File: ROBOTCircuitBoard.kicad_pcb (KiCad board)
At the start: 2 copper layers, 60.5 x 76.5 mm, 18 parts, among them J1 DB15_HighDensity_MountingHoles, J2 DB15_HighDensity_MountingHoles, P1 CONN_01X03, P13 CONN_01X04, P15 CONN_01X04, P2 CONN_01X04, P24 CONN_01X04, P3 CONN_01X04, P4 CONN_01X04, P5 CONN_01X05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

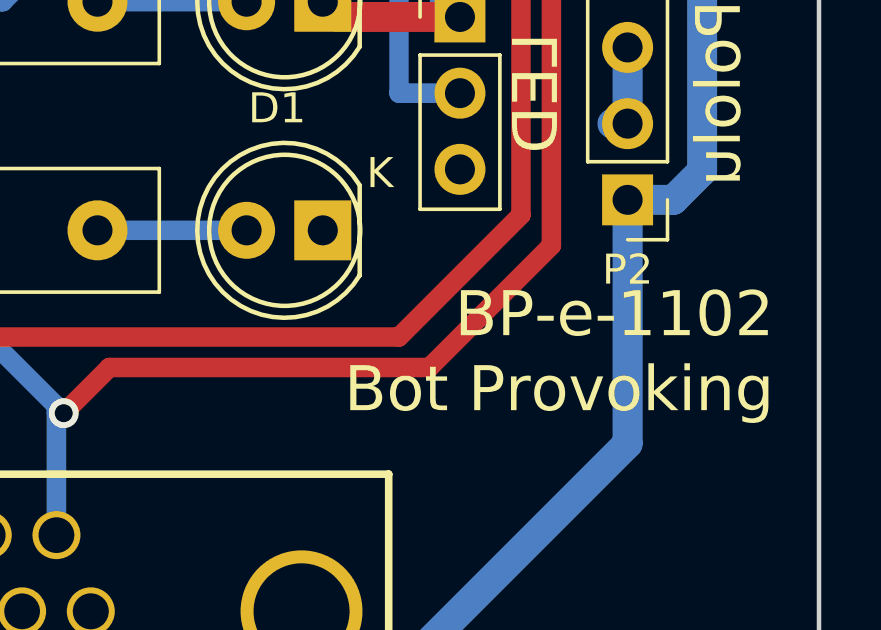
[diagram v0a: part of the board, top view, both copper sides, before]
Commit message: Fixed silkscreen and began more organized board, not used.
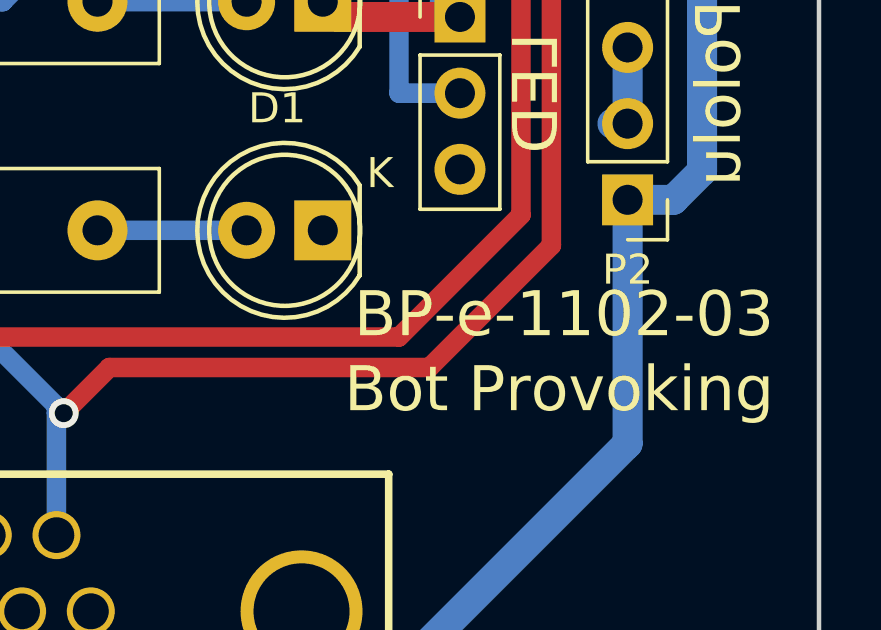
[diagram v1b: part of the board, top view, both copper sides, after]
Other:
- board text added: "BP-e-1102-03"
- board text removed: "BP-e-1102"
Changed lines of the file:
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@@
     (effects (font (size 1.5 1.5) (thickness 0.3)) (justify right))
   )
-  (gr_text BP-e-1102 (at 203 142.5) (layer F.SilkS)
+  (gr_text BP-e-1102-03 (at 203 142.5) (layer F.SilkS)
     (effects (font (size 1.5 1.5) (thickness 0.3)) (justify right))
   )
@@
     (effects (font (size 1.5 1.5) (thickness 0.3)) (justify right mirror))
   )
-  (gr_text BP-e-1102 (at 146 146.5) (layer B.SilkS)
+  (gr_text BP-e-1102-03 (at 146 146.5) (layer B.SilkS)
     (effects (font (size 1.5 1.5) (thickness 0.3)) (justify right mirror))
   )

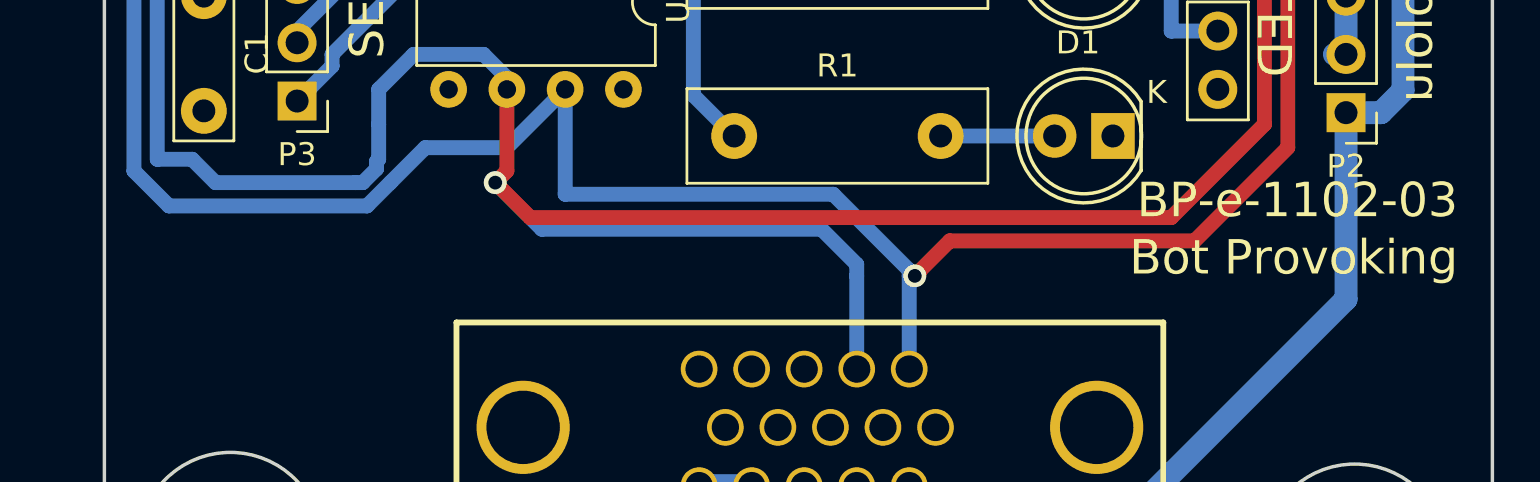
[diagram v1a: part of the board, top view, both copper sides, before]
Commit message: fixed silkscreen
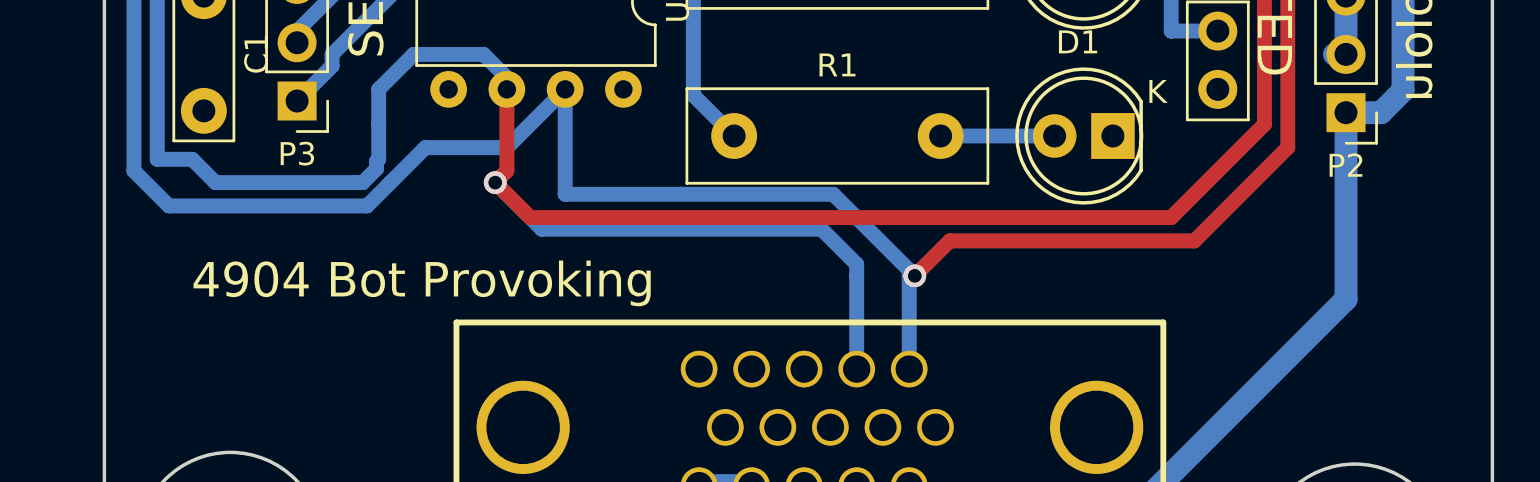
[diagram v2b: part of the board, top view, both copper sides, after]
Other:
- board text added: "4904 Bot Provoking"
- board text added: "BP-E-1102-03"
- board text removed: "BP-e-1102-03"
- board text removed: "Bot Provoking"
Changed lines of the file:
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@@
     (area 143.924999 81.206999 204.592004 170.253001)
     (thickness 1.6)
-    (drawings 20)
+    (drawings 18)
     (tracks 186)
     (zones 0)
@@
     (effects (font (size 1.5 1.5) (thickness 0.3)) (justify mirror))
   )
-  (gr_text "Bot Provoking" (at 203 145) (layer F.SilkS)
+  (gr_text "4904 Bot Provoking" (at 168 146) (layer F.SilkS)
     (effects (font (size 1.5 1.5) (thickness 0.3)) (justify right))
   )
-  (gr_text BP-e-1102-03 (at 203 142.5) (layer F.SilkS)
-    (effects (font (size 1.5 1.5) (thickness 0.3)) (justify right))
-  )
-  (gr_text "Bot Provoking" (at 146 149) (layer B.SilkS)
+  (gr_text BP-E-1102-03 (at 146 146) (layer B.SilkS)
     (effects (font (size 1.5 1.5) (thickness 0.3)) (justify right mirror))
   )
-  (gr_text BP-e-1102-03 (at 146 146.5) (layer B.SilkS)
-    (effects (font (size 1.5 1.5) (thickness 0.3)) (justify right mirror))
-  )
